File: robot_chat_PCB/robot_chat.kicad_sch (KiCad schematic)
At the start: 0 parts

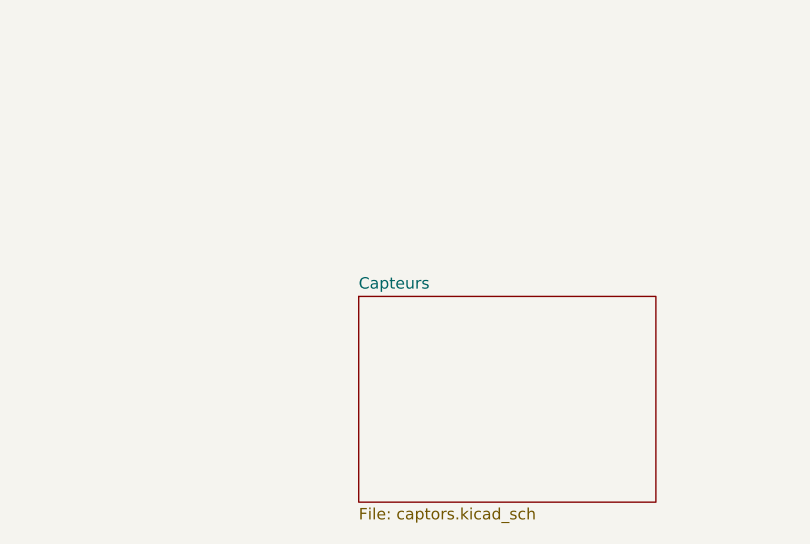
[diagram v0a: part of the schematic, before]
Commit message: pcb alim et connecteurs
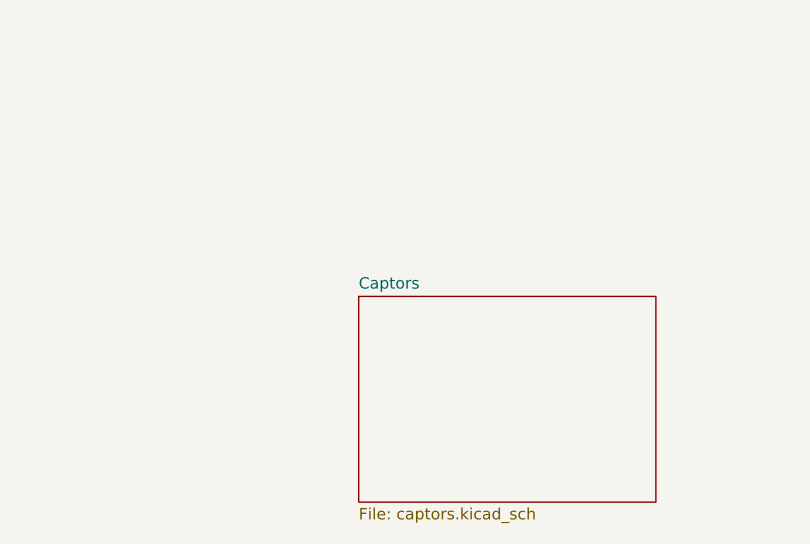
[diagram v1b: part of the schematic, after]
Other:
- sheet Capteurs renamed Captors
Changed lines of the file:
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@@
     (stroke (width 0.1524) (type solid))
     (fill (color 0 0 0 0.0000))
-    (property "Sheetname" "Capteurs" (at 80.01 123.7484 0)
+    (property "Sheetname" "Captors" (at 80.01 123.7484 0)
       (effects (font (size 1.27 1.27)) (justify left bottom))
     )
